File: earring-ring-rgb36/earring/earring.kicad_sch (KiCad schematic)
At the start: 56 parts, among them J1 Conn_01x05, Q1 AO3401A, SW1 SW_Push, U2 STM32L031G6Ux

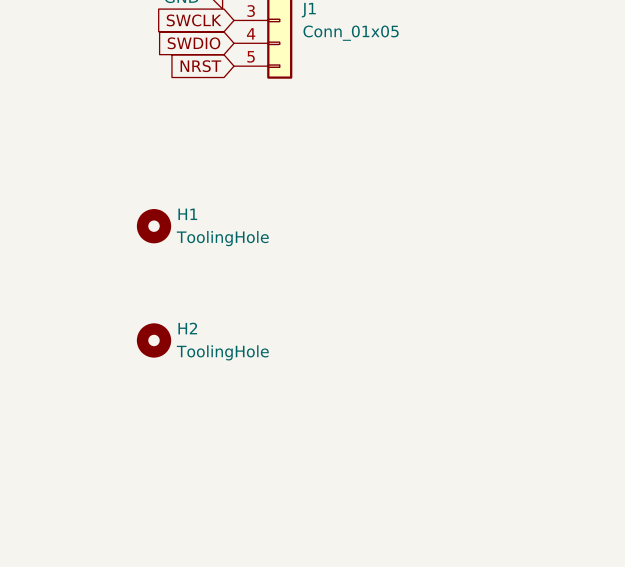
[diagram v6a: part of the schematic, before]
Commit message: earring-ring-rgb36: remove tooling holes from schematic
Also upgrade to KiCad 9.0, and maybe some other changes? (Not entirely
sure what kind of things changed, but I think this is the version that
was actually sent to JLCPCB).
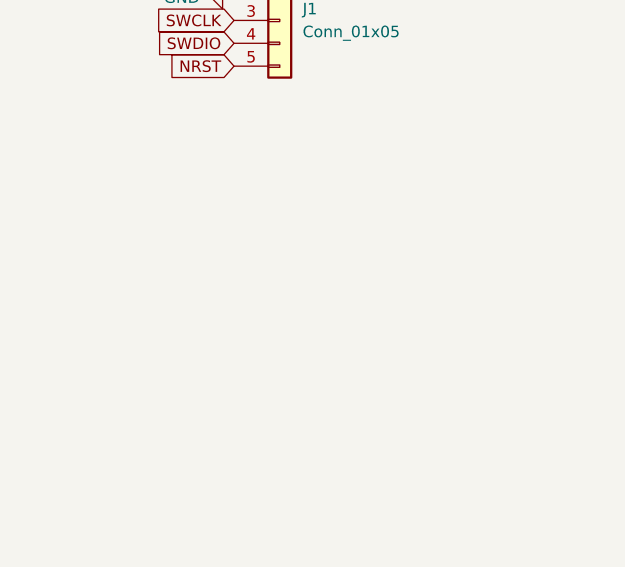
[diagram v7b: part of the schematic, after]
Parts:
- removed H1: ToolingHole, Custom:ToolingHole_JLCPCB, symbol Mechanical:MountingHole
- removed H2: ToolingHole, Custom:ToolingHoleWithMouseBytes, symbol Mechanical:MountingHole
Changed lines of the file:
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@@
-	)
-	(symbol
-		(lib_id "Mechanical:MountingHole")
-		(at 26.67 134.62 0)
-		(unit 1)
-		(exclude_from_sim no)
-		(in_bom no)
-		(on_board yes)
-		(dnp no)
-		(fields_autoplaced yes)
-		(property "Reference" "H1"
-			(at 29.21 133.3499 0)
-			(effects
-				(font
-					(size 1.27 1.27)
-				)
-				(justify left)
-			)
-		)
-		(property "Value" "ToolingHole"
-			(at 29.21 135.8899 0)
-			(effects
-				(font
-					(size 1.27 1.27)
-				)
-				(justify left)
-			)
-		)
-		(property "Footprint" "Custom:ToolingHole_JLCPCB"
-			(at 26.67 134.62 0)
-			(effects
-				(font
-					(size 1.27 1.27)
-				)
-				(hide yes)
-			)
-		)
-		(property "Datasheet" "~"
-			(at 26.67 134.62 0)
-			(effects
-				(font
-					(size 1.27 1.27)
-				)
-				(hide yes)
-			)
-		)
-		(property "Description" "Mounting Hole without connection"
-			(at 26.67 134.62 0)
-			(effects
-				(font
-					(size 1.27 1.27)
-				)
-				(hide yes)
-			)
-		)
-		(instances
-			(project ""
-				(path "/5b672b97-2486-4be1-9927-7141d9b63fb2"
-					(reference "H1")
-					(unit 1)
-				)
-			)
-		)
 	)
 	(symbol
@@
 					(unit 1)
 				)
-			)
-		)
-	)
-	(symbol
-		(lib_id "Mechanical:MountingHole")
-		(at 26.67 147.32 0)
-		(unit 1)
-		(exclude_from_sim no)
-		(in_bom no)
-		(on_board yes)
-		(dnp no)
-		(fields_autoplaced yes)
-		(property "Reference" "H2"
-			(at 29.21 146.0499 0)
-			(effects
-				(font
-					(size 1.27 1.27)
-				)
-				(justify left)
-			)
-		)
-		(property "Value" "ToolingHole"
-			(at 29.21 148.5899 0)
-			(effects
-				(font
-					(size 1.27 1.27)
-				)
-				(justify left)
-			)
-		)
-		(property "Footprint" "Custom:ToolingHoleWithMouseBytes"
-			(at 26.67 147.32 0)
-			(effects
-				(font
-					(size 1.27 1.27)
-				)
-				(hide yes)
-			)
-		)
-		(property "Datasheet" "~"
-			(at 26.67 147.32 0)
-			(effects
-				(font
-					(size 1.27 1.27)
-				)
-				(hide yes)
-			)
-		)
-		(property "Description" "Mounting Hole without connection"
-			(at 26.67 147.32 0)
-			(effects
-				(font
-					(size 1.27 1.27)
-				)
-				(hide yes)
-			)
-		)
-		(instances
-			(project "earring"
-				(path "/5b672b97-2486-4be1-9927-7141d9b63fb2"
-					(reference "H2")
-					(unit 1)
-				)
